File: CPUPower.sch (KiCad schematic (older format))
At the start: 20 parts, among them U1 IMX6UL_BGA289

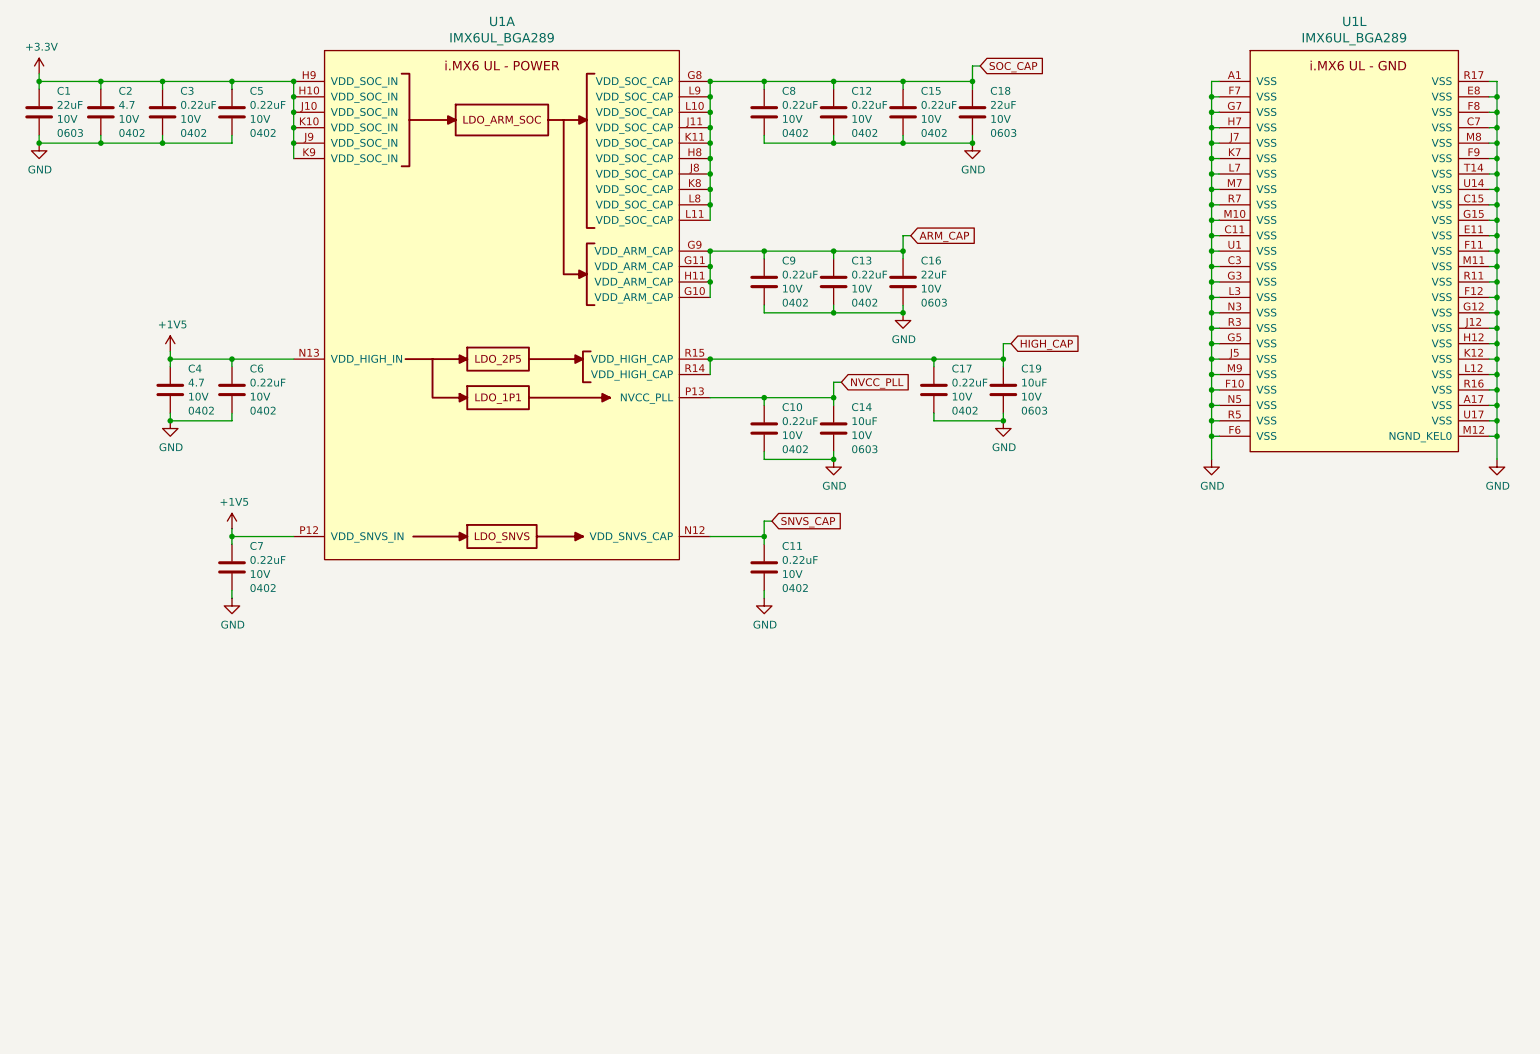
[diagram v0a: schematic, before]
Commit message: Added some LDO and connectors, still need to finish routing
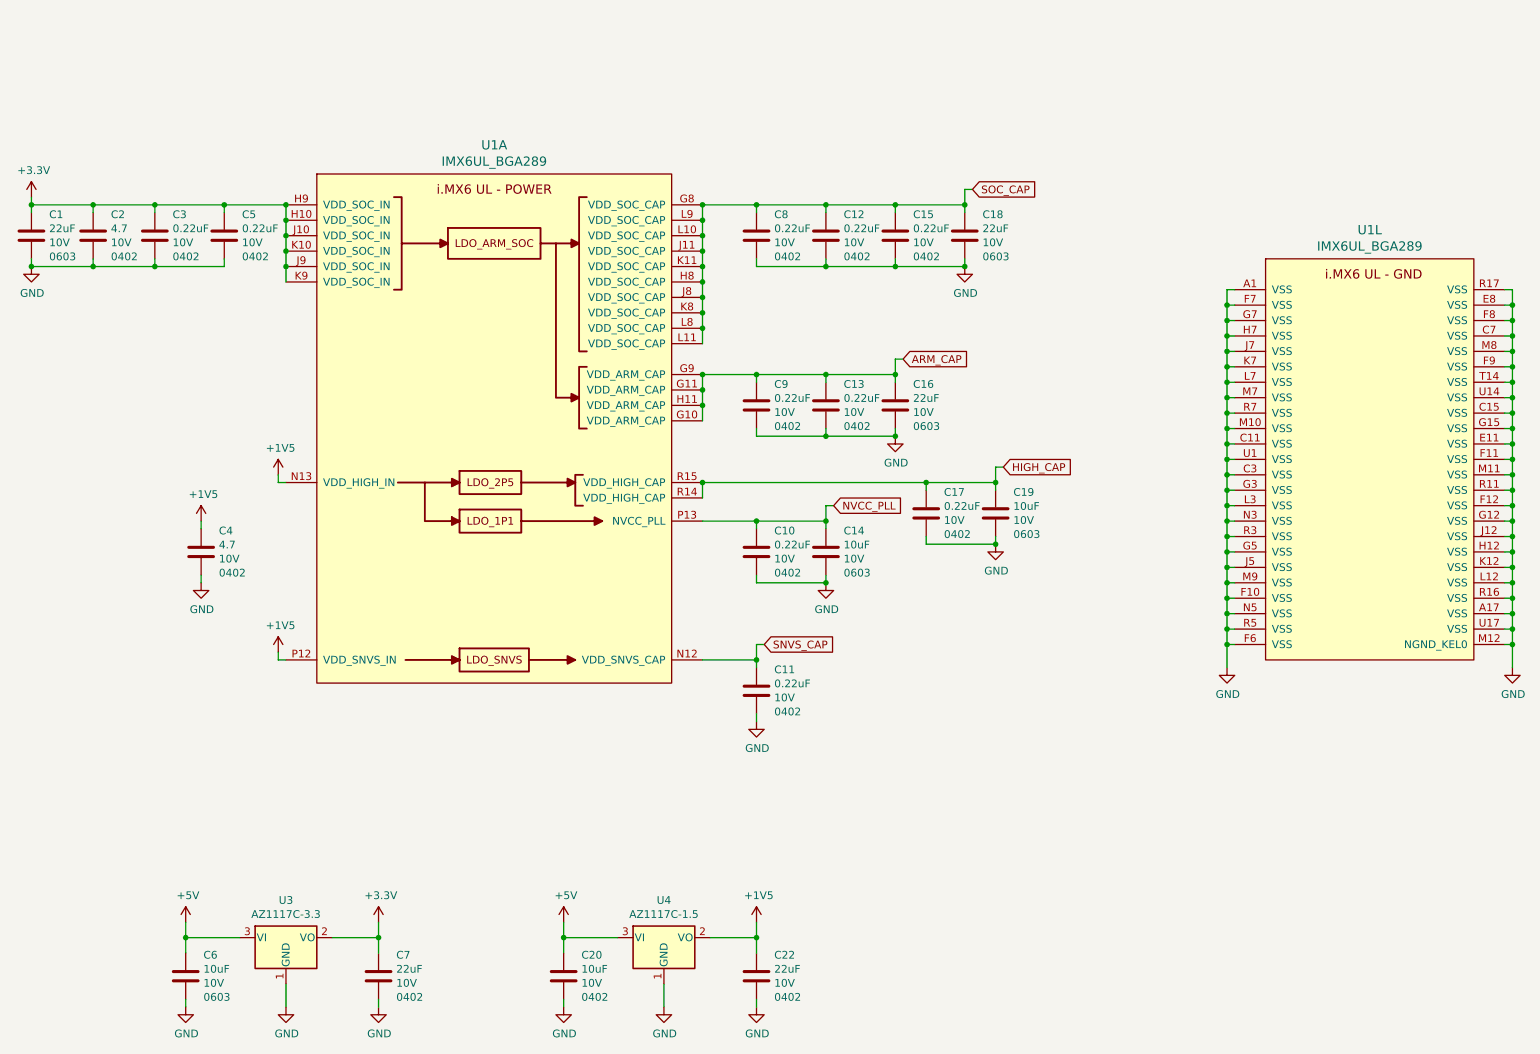
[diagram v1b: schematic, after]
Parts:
- added C20: 10uF, Capacitor_SMD:C_0402_1005Metric, symbol Device:C
- added C22: 22uF, Capacitor_SMD:C_0402_1005Metric, symbol Device:C
- added U3: AZ1117C-3.3, Package_TO_SOT_SMD:SOT-223, symbol Regulator_Linear:AZ1117-3.3
- added U4: AZ1117C-1.5, Package_TO_SOT_SMD:SOT-223, symbol Regulator_Linear:AZ1117-1.5
- C6: value 0.22uF -> 10uF; SMD 0402 -> 0603
- C7: value 0.22uF -> 22uF
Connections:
- net +1V5: now also C22.1, U4.2 (VO); no longer C6.1, C7.1
- net +3V3: now also C7.1, U3.2 (VO)
- net GND: now also C20.2, C22.2, U3.1 (GND), U4.1 (GND)
- new net +5V: C20.1, C6.1, U3.3 (VI), U4.3 (VI)
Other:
- moved on the sheet: C1, C10, C11, C12, C13, C14, C15, C16, C17, C18, C19, C2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

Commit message: Finished first version of board
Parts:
- added J3: USB_A, Connector_USB:USB_A_Molex_67643_Horizontal, symbol Connector:USB_A
- C1, C16, C18: LCSC (none) -> C59461
- C10, C11, C12, C13, C15, C17, C3, C5, C8, C9: LCSC (none) -> C16772
- C14, C19: LCSC (none) -> C15525
- C2, C4: value 4.7 -> 4.7uF; LCSC (none) -> C23733
- C20: footprint Capacitor_SMD:C_0402_1005Metric -> Capacitor_SMD:C_0603_1608Metric; LCSC (none) -> C15525; SMD 0402 -> 0603
- C22, C7: footprint Capacitor_SMD:C_0402_1005Metric -> Capacitor_SMD:C_0603_1608Metric; LCSC (none) -> C59461; SMD 0402 -> 0603
- C6: footprint Capacitor_SMD:C_0402_1005Metric -> Capacitor_SMD:C_0603_1608Metric; LCSC (none) -> C15525
- U1: LCSC (none) -> C414042
- U3: LCSC (none) -> C108492
- U4: LCSC (none) -> C92108
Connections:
- net +5V: now also J3.1 (VBUS)
- net GND: now also J3.4 (GND), J3.5 (Shield)
- no-connect marks 0 -> 2
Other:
- moved on the sheet: C1, C10, C11, C12, C13, C14, C15, C16, C17, C18, C19, C2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
